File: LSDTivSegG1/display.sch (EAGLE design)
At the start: 95 parts, among them IC1 MEGA8-P, IC2 MAX232, IC3 PCF8574P, IC4 PCF8574P, IC5 PCF8574P, IC6 PCF8574P

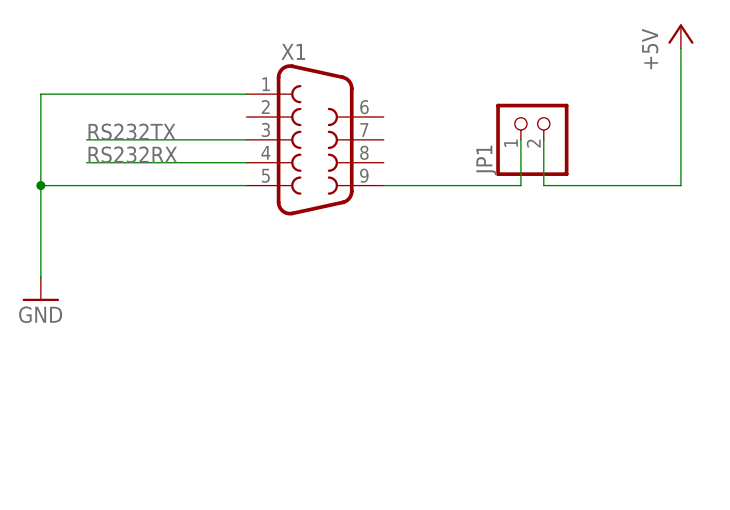
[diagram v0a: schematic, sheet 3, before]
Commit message: added RS232 crossing pinhead
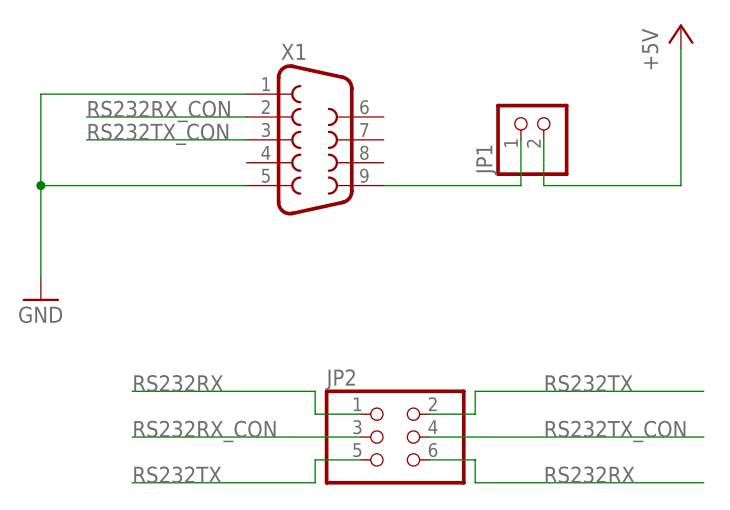
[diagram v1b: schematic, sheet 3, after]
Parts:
- added JP2: (no value), pinhead:PINHD-2X3
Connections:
- new net RS232RX_CON: JP2.3, X1.2
- new net RS232TX_CON: JP2.4, X1.3
- net RS232RX: now also JP2.1, JP2.6; no longer X1.4
- net RS232TX: now also JP2.2, JP2.5; no longer X1.3
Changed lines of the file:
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@@
 <part name="FRAME7" library="frames" library_urn="urn:adsk.eagle:library:229" deviceset="A4P-LOC" device=""/>
 <part name="JP1" library="pinhead" library_urn="urn:adsk.eagle:library:325" deviceset="PINHD-1X2" device="" package3d_urn="urn:adsk.eagle:package:22435/2"/>
+<part name="JP2" library="pinhead" library_urn="urn:adsk.eagle:library:325" deviceset="PINHD-2X3" device="" package3d_urn="urn:adsk.eagle:package:22462/2"/>
 </parts>
 <sheets>
@@
 <instance part="FRAME3" gate="G$1" x="-88.9" y="-101.6"/>
 <instance part="JP1" gate="G$1" x="55.88" y="-10.16" rot="R90"/>
+<instance part="JP2" gate="A" x="38.1" y="-45.72"/>
 </instances>
 <busses>
 </busses>
 <nets>
-<net name="RS232TX" class="0">
-<segment>
-<pinref part="X1" gate="G$1" pin="3"/>
-<wire x1="22.86" y1="-12.7" x2="5.08" y2="-12.7" width="0.1524" layer="91"/>
-<label x="5.08" y="-12.7" size="1.778" layer="95"/>
-</segment>
-</net>
-<net name="RS232RX" class="0">
-<segment>
-<pinref part="X1" gate="G$1" pin="4"/>
-<wire x1="22.86" y1="-15.24" x2="5.08" y2="-15.24" width="0.1524" layer="91"/>
-<label x="5.08" y="-15.24" size="1.778" layer="95"/>
-</segment>
-</net>
 <net name="GND" class="0">
 <segment>
@@
 </segment>
 </net>
+<net name="RS232RX_CON" class="0">
+<segment>
+<pinref part="X1" gate="G$1" pin="2"/>
+<wire x1="22.86" y1="-10.16" x2="5.08" y2="-10.16" width="0.1524" layer="91"/>
+<label x="5.08" y="-10.16" size="1.778" layer="95"/>
+</segment>
+<segment>
+<pinref part="JP2" gate="A" pin="3"/>
+<wire x1="35.56" y1="-45.72" x2="10.16" y2="-45.72" width="0.1524" layer="91"/>
+<label x="10.16" y="-45.72" size="1.778" layer="95"/>
+</segment>
+</net>
+<net name="RS232TX_CON" class="0">
+<segment>
+<pinref part="X1" gate="G$1" pin="3"/>
+<wire x1="22.86" y1="-12.7" x2="5.08" y2="-12.7" width="0.1524" layer="91"/>
+<label x="5.08" y="-12.7" size="1.778" layer="95"/>
+</segment>
+<segment>
+<pinref part="JP2" gate="A" pin="4"/>
+<wire x1="43.18" y1="-45.72" x2="73.66" y2="-45.72" width="0.1524" layer="91"/>
+<label x="55.88" y="-45.72" size="1.778" layer="95"/>
+</segment>
+</net>
+<net name="RS232RX" class="0">
+<segment>
+<pinref part="JP2" gate="A" pin="1"/>
+<wire x1="35.56" y1="-43.18" x2="30.48" y2="-43.18" width="0.1524" layer="91"/>
+<wire x1="30.48" y1="-43.18" x2="30.48" y2="-40.64" width="0.1524" layer="91"/>
+<wire x1="30.48" y1="-40.64" x2="10.16" y2="-40.64" width="0.1524" layer="91"/>
+<label x="10.16" y="-40.64" size="1.778" layer="95"/>
+</segment>
+<segment>
+<pinref part="JP2" gate="A" pin="6"/>
+<wire x1="43.18" y1="-48.26" x2="48.26" y2="-48.26" width="0.1524" layer="91"/>
+<wire x1="48.26" y1="-48.26" x2="48.26" y2="-50.8" width="0.1524" layer="91"/>
+<wire x1="48.26" y1="-50.8" x2="73.66" y2="-50.8" width="0.1524" layer="91"/>
+<label x="55.88" y="-50.8" size="1.778" layer="95"/>
+</segment>
+</net>
+<net name="RS232TX" class="0">
+<segment>
+<pinref part="JP2" gate="A" pin="5"/>
+<wire x1="35.56" y1="-48.26" x2="30.48" y2="-48.26" width="0.1524" layer="91"/>
+<wire x1="30.48" y1="-48.26" x2="30.48" y2="-50.8" width="0.1524" layer="91"/>
+<wire x1="30.48" y1="-50.8" x2="10.16" y2="-50.8" width="0.1524" layer="91"/>
+<label x="10.16" y="-50.8" size="1.778" layer="95"/>
+</segment>
+<segment>
+<pinref part="JP2" gate="A" pin="2"/>
+<wire x1="43.18" y1="-43.18" x2="48.26" y2="-43.18" width="0.1524" layer="91"/>
+<wire x1="48.26" y1="-43.18" x2="48.26" y2="-40.64" width="0.1524" layer="91"/>
+<wire x1="48.26" y1="-40.64" x2="73.66" y2="-40.64" width="0.1524" layer="91"/>
+<label x="55.88" y="-40.64" size="1.778" layer="95"/>
+</segment>
+</net>

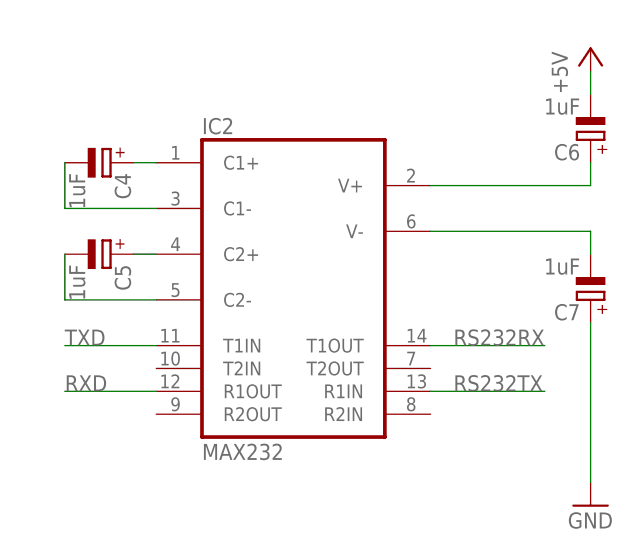
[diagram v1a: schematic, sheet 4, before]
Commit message: added supply pins to max232
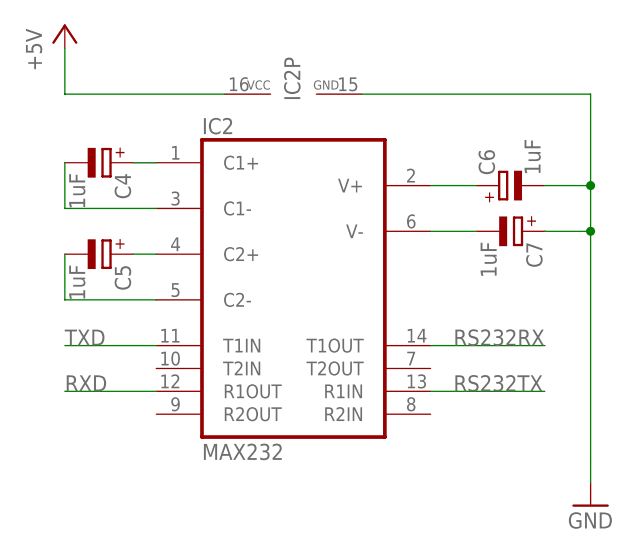
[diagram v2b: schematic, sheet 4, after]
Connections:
- net +5V: now also IC2P.VCC; no longer C6.-
- net GND: now also C6.-, IC2P.GND
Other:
- moved on the sheet: C6, C7
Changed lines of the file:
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@@
 <instances>
 <instance part="IC2" gate="G$1" x="10.16" y="17.78"/>
-<instance part="P+4" gate="1" x="43.18" y="43.18"/>
+<instance part="P+4" gate="1" x="-15.24" y="45.72"/>
 <instance part="GND5" gate="1" x="43.18" y="-7.62"/>
 <instance part="C4" gate="G$1" x="-10.16" y="30.48" rot="R270"/>
 <instance part="C5" gate="G$1" x="-10.16" y="20.32" rot="R270"/>
-<instance part="C6" gate="G$1" x="43.18" y="33.02" rot="R180"/>
-<instance part="C7" gate="G$1" x="43.18" y="15.24" rot="R180"/>
+<instance part="C6" gate="G$1" x="33.02" y="27.94" rot="R90"/>
+<instance part="C7" gate="G$1" x="35.56" y="22.86" rot="R270"/>
 <instance part="FRAME4" gate="G$1" x="-114.3" y="-76.2"/>
+<instance part="IC2" gate="P" x="10.16" y="38.1" rot="R90"/>
 </instances>
 <busses>
@@
 </segment>
 </net>
-<net name="+5V" class="0">
-<segment>
-<pinref part="C6" gate="G$1" pin="-"/>
-<pinref part="P+4" gate="1" pin="+5V"/>
-<wire x1="43.18" y1="38.1" x2="43.18" y2="40.64" width="0.1524" layer="91"/>
-</segment>
-</net>
 <net name="RXD" class="0">
 <segment>
@@
 </segment>
 </net>
+<net name="GND" class="0">
+<segment>
+<pinref part="GND5" gate="1" pin="GND"/>
+<wire x1="43.18" y1="-2.54" x2="43.18" y2="-5.08" width="0.1524" layer="91"/>
+<pinref part="C7" gate="G$1" pin="+"/>
+<wire x1="38.1" y1="22.86" x2="43.18" y2="22.86" width="0.1524" layer="91"/>
+<wire x1="43.18" y1="22.86" x2="43.18" y2="-2.54" width="0.1524" layer="91"/>
+<pinref part="C6" gate="G$1" pin="-"/>
+<wire x1="38.1" y1="27.94" x2="43.18" y2="27.94" width="0.1524" layer="91"/>
+<wire x1="43.18" y1="27.94" x2="43.18" y2="22.86" width="0.1524" layer="91"/>
+<junction x="43.18" y="22.86"/>
+<pinref part="IC2" gate="P" pin="GND"/>
+<wire x1="17.78" y1="38.1" x2="43.18" y2="38.1" width="0.1524" layer="91"/>
+<wire x1="43.18" y1="38.1" x2="43.18" y2="27.94" width="0.1524" layer="91"/>
+<junction x="43.18" y="27.94"/>
+</segment>
+</net>
 <net name="N$7" class="0">
 <segment>
 <pinref part="IC2" gate="G$1" pin="V+"/>
 <pinref part="C6" gate="G$1" pin="+"/>
-<wire x1="25.4" y1="27.94" x2="43.18" y2="27.94" width="0.1524" layer="91"/>
-<wire x1="43.18" y1="27.94" x2="43.18" y2="30.48" width="0.1524" layer="91"/>
+<wire x1="25.4" y1="27.94" x2="30.48" y2="27.94" width="0.1524" layer="91"/>
 </segment>
 </net>
@@
 <segment>
 <pinref part="IC2" gate="G$1" pin="V-"/>
-<wire x1="25.4" y1="22.86" x2="43.18" y2="22.86" width="0.1524" layer="91"/>
 <pinref part="C7" gate="G$1" pin="-"/>
-<wire x1="43.18" y1="22.86" x2="43.18" y2="20.32" width="0.1524" layer="91"/>
+<wire x1="25.4" y1="22.86" x2="30.48" y2="22.86" width="0.1524" layer="91"/>
 </segment>
 </net>
-<net name="GND" class="0">
+<net name="+5V" class="0">
 <segment>
-<pinref part="C7" gate="G$1" pin="+"/>
-<pinref part="GND5" gate="1" pin="GND"/>
-<wire x1="43.18" y1="12.7" x2="43.18" y2="-5.08" width="0.1524" layer="91"/>
+<pinref part="P+4" gate="1" pin="+5V"/>
+<pinref part="IC2" gate="P" pin="VCC"/>
+<wire x1="-15.24" y1="43.18" x2="-15.24" y2="38.1" width="0.1524" layer="91"/>
+<wire x1="-15.24" y1="38.1" x2="2.54" y2="38.1" width="0.1524" layer="91"/>
 </segment>
 </net>
